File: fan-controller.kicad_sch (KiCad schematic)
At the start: 15 parts, among them J1 PWR, J2 PTC, J3 FAN, J4 Conn_ARM_SWD_TagConnect_TC203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, Q1 AO3401A, U1 PY32F002A, U2 L78L05

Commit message: hardware bug fixes
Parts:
- added R4: 47k, Resistor_SMD:R_0402_1005Metric, symbol Device:R
- R1: renamed from R2; footprint Resistor_SMD:R_0603_1608Metric -> Resistor_SMD:R_0402_1005Metric; LCSC C25803 -> (none)
- R2: renamed from R3; footprint Resistor_SMD:R_0603_1608Metric -> Resistor_SMD:R_0402_1005Metric
- R3: renamed from R1; footprint Resistor_SMD:R_0603_1608Metric -> Resistor_SMD:R_0402_1005Metric
- renumbered C4 to C1, C1 to C2, D2 to D1, U2 to U1, U1 to U2
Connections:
- net +3.3V: now also R4.2; no longer U2.6 (PA2/PF2/~{RESET})
- net SWCLK: now also J4.4 (SWCLK); no longer J4.2 (SWDIO)
- net SWDIO: now also J4.2 (SWDIO); no longer J4.4 (SWCLK)
- net ~{RST}: now reaches J4.3 (~{RESET})
- net ~{RST}: now also J4.6 (SWO), U2.6 (PA2/PF2/~{RESET}), R4.1
- no-connect marks 2 -> 0
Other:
- note added: "for routing"

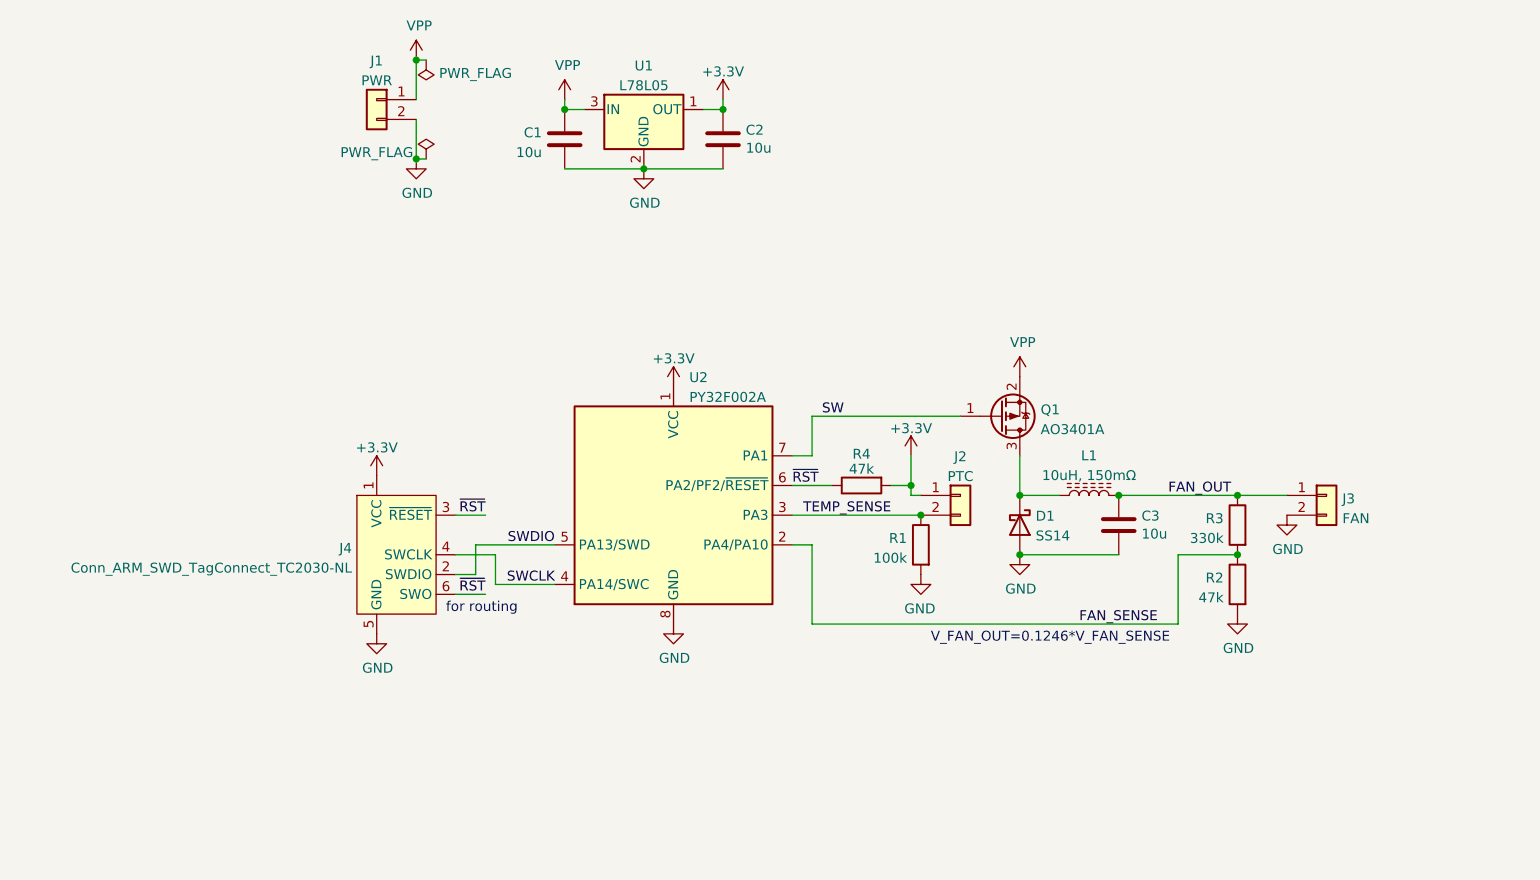
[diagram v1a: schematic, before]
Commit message: Fix circuit mistakes
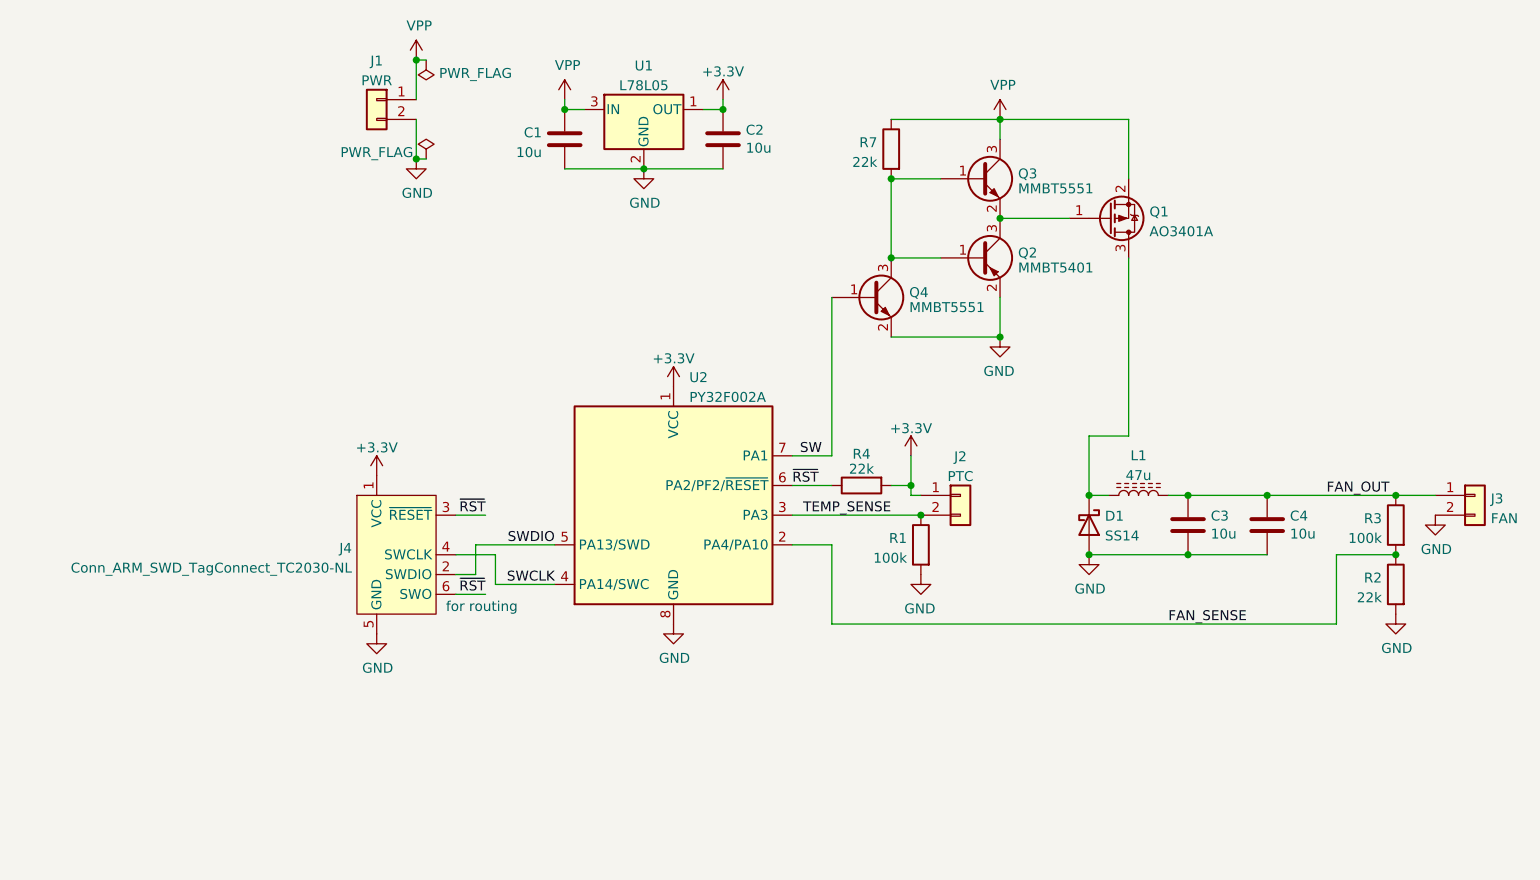
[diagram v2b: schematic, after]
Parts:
- added C4: 10u, Resistor_SMD:R_1206_3216Metric, symbol Device:C
- added Q2: MMBT5401, Package_TO_SOT_SMD:SOT-23, symbol Device:Q_PNP_BEC
- added Q3, Q4: MMBT5551, Package_TO_SOT_SMD:SOT-23, symbol Device:Q_NPN_BEC
- added R7: 22k, Resistor_SMD:R_0402_1005Metric, symbol Device:R
- L1: value 10uH, 150mΩ -> 47u; LCSC C38117 -> C54731
- R1: LCSC (none) -> C25086
- R2, R4: value 47k -> 22k; LCSC (none) -> C25768
- R3: value 330k -> 100k; LCSC (none) -> C25086
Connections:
- net FAN_OUT: now also C4.1
- net GND: now also C4.2, Q2.2 (E), Q4.2 (E)
- net SW: now also Q4.1 (B); no longer Q1.1 (G)
- net VPP: now also Q3.3 (C), R7.1
- new net: Q2.1 (B), Q3.1 (B), Q4.3 (C), R7.2
- new net: Q1.1 (G), Q2.3 (C), Q3.2 (E)
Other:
- note removed: "V_FAN_OUT=0.1246*V_FAN_SENSE"
- moved on the sheet: C3, D1, J3, L1, Q1, R2, R3

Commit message: Fix some bugs & add PWM jumper
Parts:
- added JP1: PWM_MODE, Jumper:SolderJumper-2_P1.3mm_Open_TrianglePad1.0x1.5mm, symbol Jumper:SolderJumper_2_Open
- Q2: LCSC (none) -> C8326
- Q3, Q4: LCSC (none) -> C2145
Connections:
- net FAN_OUT: now also JP1.2 (B)
- net at D1.1 (K), L1.1, Q1.3 (D): now also JP1.1 (A)
- net +3.3V renamed +5V
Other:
- note added: "Bypass the inductor for 3-pin fans"

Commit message: Simplify circuit
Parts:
- removed JP1: PWM_MODE, Jumper:SolderJumper-2_P1.3mm_Open_TrianglePad1.0x1.5mm, symbol Jumper:SolderJumper_2_Open
- removed Q1: AO3401A, Package_TO_SOT_SMD:SOT-23, symbol Transistor_FET:AO3401A
- removed Q2: MMBT5401, Package_TO_SOT_SMD:SOT-23, symbol Device:Q_PNP_BEC
- removed Q3, Q4: MMBT5551, Package_TO_SOT_SMD:SOT-23, symbol Device:Q_NPN_BEC
- removed R7: 22k, Resistor_SMD:R_0402_1005Metric, symbol Device:R
- added Q5: AO3400A, Package_TO_SOT_SMD:SOT-23, symbol Transistor_FET:AO3400A
- added R5: 100, Resistor_SMD:R_0402_1005Metric, symbol Device:R
- R2: value 22k -> 100k; LCSC C25768 -> C25086
- R3: value 100k -> 22k; LCSC C25086 -> C25768
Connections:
- net GND: now also R3.1, Q5.2 (S); no longer D1.2 (A), J3.2 (Pin_2), R2.2
- net SW: now also R5.1
- net VPP: now also J3.1 (Pin_1)
- net ~{RST}: no longer J4.6 (SWO)
- net at L1.1: now also D1.2 (A), Q5.3 (D); no longer D1.1 (K)
- net FAN_OUT renamed FAN_OUT-
- net FAN_OUT-: now also D1.1 (K), J3.2 (Pin_2), R2.1; no longer J3.1 (Pin_1), R3.1
- net FAN_SENSE: no longer names the net of R3.2, U2.2 (PA4/PA10)
- net FAN_SENSE: now also R2.2; no longer R2.1
- new net: Q5.1 (G), R5.2
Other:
- note removed: "Bypass the inductor for 3-pin fans"
- note removed: "for routing"
- moved on the sheet: C3, C4, D1, J3, L1

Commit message: Fix dumb errors (wrong part #)
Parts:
- removed R2: 100k, Resistor_SMD:R_0402_1005Metric, symbol Device:R
- removed R3: 22k, Resistor_SMD:R_0402_1005Metric, symbol Device:R
- R1: LCSC C25086 -> C25741
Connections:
- no-connect marks 0 -> 1
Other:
- moved on the sheet: J3
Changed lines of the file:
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@@
   (junction (at 158.75 78.74) (diameter 0) (color 0 0 0 0)
   )
-  (junction (at 182.88 88.9) (diameter 0) (color 0 0 0 0)
-  )
-  (junction (at 191.77 78.74) (diameter 0) (color 0 0 0 0)
-  )
   (junction (at 109.22 49.53) (diameter 0) (color 0 0 0 0)
   )
   (junction (at 90.17 55.88) (diameter 0) (color 0 0 0 0)
   )
-  (junction (at 191.77 71.12) (diameter 0) (color 0 0 0 0)
-  )
   (junction (at 129.54 49.53) (diameter 0) (color 0 0 0 0)
   )
   (junction (at 154.94 101.6) (diameter 0) (color 0 0 0 0)
   )
+  (no_connect (at 138.43 105.41))
   (wire (pts (xy 127 49.53) (xy 129.54 49.53))
     (stroke (width 0) (type default))
@@
     (stroke (width 0) (type default))
   )
-  (wire (pts (xy 191.77 71.12) (xy 194.31 71.12))
-    (stroke (width 0) (type default))
-  )
   (wire (pts (xy 129.54 48.26) (xy 129.54 49.53))
     (stroke (width 0) (type default))
   )
-  (wire (pts (xy 191.77 78.74) (xy 198.12 78.74))
-    (stroke (width 0) (type default))
-  )
   (wire (pts (xy 138.43 93.98) (xy 143.51 93.98))
     (stroke (width 0) (type default))
@@
     (stroke (width 0) (type default))
   )
+  (wire (pts (xy 165.1 71.12) (xy 175.26 71.12))
+    (stroke (width 0) (type default))
+  )
   (wire (pts (xy 138.43 101.6) (xy 154.94 101.6))
     (stroke (width 0) (type default))
   )
-  (wire (pts (xy 198.12 114.3) (xy 139.7 114.3))
-    (stroke (width 0) (type default))
-  )
   (wire (pts (xy 90.17 55.88) (xy 91.44 55.88))
     (stroke (width 0) (type default))
@@
     (stroke (width 0) (type default))
   )
-  (wire (pts (xy 182.88 88.9) (xy 191.77 88.9))
-    (stroke (width 0) (type default))
-  )
   (wire (pts (xy 95.25 101.6) (xy 99.06 101.6))
     (stroke (width 0) (type default))
@@
     (stroke (width 0) (type default))
   )
-  (wire (pts (xy 191.77 88.9) (xy 191.77 86.36))
-    (stroke (width 0) (type default))
-  )
   (wire (pts (xy 182.88 88.9) (xy 182.88 86.36))
     (stroke (width 0) (type default))
@@
     (stroke (width 0) (type default))
   )
-  (wire (pts (xy 198.12 78.74) (xy 198.12 114.3))
-    (stroke (width 0) (type default))
-  )
   (wire (pts (xy 182.88 71.12) (xy 182.88 78.74))
     (stroke (width 0) (type default))
@@
     (stroke (width 0) (type default))
   )
-  (wire (pts (xy 139.7 105.41) (xy 138.43 105.41))
-    (stroke (width 0) (type default))
-  )
   (wire (pts (xy 90.17 50.8) (xy 90.17 55.88))
     (stroke (width 0) (type default))
   )
-  (wire (pts (xy 139.7 105.41) (xy 139.7 114.3))
+  (wire (pts (xy 182.88 71.12) (xy 184.15 71.12))
     (stroke (width 0) (type default))
   )
@@
   )
   (wire (pts (xy 158.75 71.12) (xy 165.1 71.12))
-    (stroke (width 0) (type default))
-  )
-  (wire (pts (xy 165.1 71.12) (xy 175.26 71.12))
-    (stroke (width 0) (type default))
-  )
-  (wire (pts (xy 191.77 71.12) (xy 182.88 71.12))
     (stroke (width 0) (type default))
   )
@@
     )
   )
-  (symbol (lib_id "Device:R") (at 191.77 74.93 0) (mirror y) (unit 1)
-    (in_bom yes) (on_board yes) (dnp no) (fields_autoplaced)
-    (property "Reference" "R2" (at 193.548 73.906 0)
-      (effects (font (size 1.27 1.27)) (justify right))
-    )
-    (property "Value" "100k" (at 193.548 75.954 0)
-      (effects (font (size 1.27 1.27)) (justify right))
-    )
-    (property "Footprint" "Resistor_SMD:R_0402_1005Metric" (at 193.548 74.93 90)
-      (effects (font (size 1.27 1.27)) hide)
-    )
-    (property "Datasheet" "~" (at 191.77 74.93 0)
-      (effects (font (size 1.27 1.27)) hide)
-    )
-    (property "LCSC" "C25086" (at 191.77 74.93 0)
-      (effects (font (size 1.27 1.27)) hide)
-    )
-    (pin "1")
-    (pin "2")
-    (instances
-      (project "fan-controller"
-        (path "/b4621266-bc2f-4576-8714-caa2a8246339"
-          (reference "R2") (unit 1)
-        )
-      )
-    )
-  )
   (symbol (lib_id "power:+5V") (at 129.54 48.26 0) (unit 1)
     (in_bom yes) (on_board yes) (dnp no) (fields_autoplaced)
@@
         (path "/b4621266-bc2f-4576-8714-caa2a8246339"
           (reference "#PWR013") (unit 1)
-        )
-      )
-    )
-  )
-  (symbol (lib_id "Device:R") (at 191.77 82.55 0) (mirror x) (unit 1)
-    (in_bom yes) (on_board yes) (dnp no) (fields_autoplaced)
-    (property "Reference" "R3" (at 193.548 81.526 0)
-      (effects (font (size 1.27 1.27)) (justify left))
-    )
-    (property "Value" "22k" (at 193.548 83.574 0)
-      (effects (font (size 1.27 1.27)) (justify left))
-    )
-    (property "Footprint" "Resistor_SMD:R_0402_1005Metric" (at 189.992 82.55 90)
-      (effects (font (size 1.27 1.27)) hide)
-    )
-    (property "Datasheet" "~" (at 191.77 82.55 0)
-      (effects (font (size 1.27 1.27)) hide)
-    )
-    (property "LCSC" "C25768" (at 191.77 82.55 0)
-      (effects (font (size 1.27 1.27)) hide)
-    )
-    (pin "1")
-    (pin "2")
-    (instances
-      (project "fan-controller"
-        (path "/b4621266-bc2f-4576-8714-caa2a8246339"
-          (reference "R3") (unit 1)
         )
       )
@@
     )
   )
-  (symbol (lib_id "power:VPP") (at 194.31 68.58 0) (unit 1)
-    (in_bom yes) (on_board yes) (dnp no)
-    (property "Reference" "#PWR03" (at 194.31 72.39 0)
-      (effects (font (size 1.27 1.27)) hide)
-    )
-    (property "Value" "VPP" (at 194.691 64.1858 0)
-      (effects (font (size 1.27 1.27)))
-    )
-    (property "Footprint" "" (at 194.31 68.58 0)
-      (effects (font (size 1.27 1.27)) hide)
-    )
-    (property "Datasheet" "" (at 194.31 68.58 0)
+  (symbol (lib_id "power:VPP") (at 184.15 68.58 0) (unit 1)
+    (in_bom yes) (on_board yes) (dnp no)
+    (property "Reference" "#PWR03" (at 184.15 72.39 0)
+      (effects (font (size 1.27 1.27)) hide)
+    )
+    (property "Value" "VPP" (at 184.531 64.1858 0)
+      (effects (font (size 1.27 1.27)))
+    )
+    (property "Footprint" "" (at 184.15 68.58 0)
+      (effects (font (size 1.27 1.27)) hide)
+    )
+    (property "Datasheet" "" (at 184.15 68.58 0)
       (effects (font (size 1.27 1.27)) hide)
     )
@@
       (effects (font (size 1.27 1.27)) hide)
     )
-    (property "LCSC" "C25086" (at 154.94 105.41 0)
+    (property "LCSC" "C25741" (at 154.94 105.41 0)
       (effects (font (size 1.27 1.27)) hide)
     )
@@
     )
   )
-  (symbol (lib_id "Connector_Generic:Conn_01x02") (at 199.39 68.58 0) (unit 1)
-    (in_bom yes) (on_board yes) (dnp no) (fields_autoplaced)
-    (property "Reference" "J3" (at 201.422 69.0153 0)
-      (effects (font (size 1.27 1.27)) (justify left))
-    )
-    (property "Value" "FAN" (at 201.422 71.5522 0)
-      (effects (font (size 1.27 1.27)) (justify left))
-    )
-    (property "Footprint" "Connector_PinHeader_2.54mm:PinHeader_1x02_P2.54mm_Vertical" (at 199.39 68.58 0)
-      (effects (font (size 1.27 1.27)) hide)
-    )
-    (property "Datasheet" "~" (at 199.39 68.58 0)
-      (effects (font (size 1.27 1.27)) hide)
-    )
+  (symbol (lib_id "Connector_Generic:Conn_01x02") (at 189.23 68.58 0) (unit 1)
+    (in_bom yes) (on_board yes) (dnp no) (fields_autoplaced)
+    (property "Reference" "J3" (at 191.262 69.0153 0)
+      (effects (font (size 1.27 1.27)) (justify left))
+    )
+    (property "Value" "FAN" (at 191.262 71.5522 0)
+      (effects (font (size 1.27 1.27)) (justify left))
+    )
+    (property "Footprint" "Connector_PinHeader_2.54mm:PinHeader_1x02_P2.54mm_Vertical" (at 189.23 68.58 0)
+      (effects (font (size 1.27 1.27)) hide)
+    )
+    (property "Datasheet" "~" (at 189.23 68.58 0)
+      (effects (font (size 1.27 1.27)) hide)
+    )

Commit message: Improve hardware reliability
Current sense + low-pass temperature filter at 100Hz cutoff
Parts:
- added C5, C6: 10n, Resistor_SMD:R_0402_1005Metric, symbol Device:C
- added J5: Conn_01x04, Connector_PinHeader_2.54mm:PinHeader_1x04_P2.54mm_Vertical, symbol Connector_Generic:Conn_01x04
- added R2: 1, Resistor_SMD:R_0805_2012Metric, symbol Device:R
- added R3: 100k, Resistor_SMD:R_0402_1005Metric, symbol Device:R
- D1: value SS14 -> 1N5819WS; footprint Diode_SMD:D_SMA -> Diode_SMD:D_SOD-323_HandSoldering; LCSC C2480 -> C191023
- J1, J2, J3: footprint Connector_PinHeader_2.54mm:PinHeader_1x02_P2.54mm_Vertical -> Connector_JST:JST_XH_S2B-XH-A_1x02_P2.50mm_Horizontal
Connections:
- net +5V: now also J5.1 (Pin_1)
- net GND: now also C5.2, C6.2, J5.2 (Pin_2), R2.1; no longer Q5.2 (S)
- net SWCLK: now also J5.3 (Pin_3)
- net SWDIO: now also J5.4 (Pin_4)
- net TEMP_SENSE: now also C6.1
- net ISENSE: now reaches U2.2 (PA4/PA10)
- net ISENSE: now also C5.1, R3.2
- new net: Q5.2 (S), R2.2, R3.1
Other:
- note added: "programing port for users without tagconnect"
- moved on the sheet: C3, C4, D1, J2, J3, L1, Q5, R1

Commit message: Update LCSC part numbers
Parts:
- C5, C6: LCSC (none) -> C15195
- J1, J2, J3: LCSC (none) -> C163035
- R2: LCSC (none) -> C25271
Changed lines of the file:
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@@
       (effects (font (size 1.27 1.27)) hide)
     )
-    (property "LCSC" "" (at 153.67 105.41 0)
+    (property "LCSC" "C15195" (at 153.67 105.41 0)
       (effects (font (size 1.27 1.27)) hide)
     )
@@
       (effects (font (size 1.27 1.27)) hide)
     )
+    (property "LCSC" "C163035" (at 168.91 99.06 0)
+      (effects (font (size 1.27 1.27)) hide)
+    )
     (pin "1")
     (pin "2")
@@
       (effects (font (size 1.27 1.27)) hide)
     )
+    (property "LCSC" "C163035" (at 214.63 68.58 0)
+      (effects (font (size 1.27 1.27)) hide)
+    )
     (pin "1")
     (pin "2")
@@
       (effects (font (size 1.27 1.27)) hide)
     )
+    (property "LCSC" "C163035" (at 85.09 48.26 0)
+      (effects (font (size 1.27 1.27)) hide)
+    )
     (pin "1")
     (pin "2")
@@
       (effects (font (size 1.27 1.27)) hide)
     )
-    (property "LCSC" "" (at 185.42 99.06 0)
+    (property "LCSC" "C15195" (at 185.42 99.06 0)
       (effects (font (size 1.27 1.27)) hide)
     )
@@
       (effects (font (size 1.27 1.27)) hide)
     )
-    (property "LCSC" "" (at 177.8 99.06 0)
-      (effects (font (size 1.27 1.27)) hide)
-    )
+    (property "LCSC" "C25271" (at 177.8 99.06 0)
+      (effects (font (size 1.27 1.27)) hide)
+    )
